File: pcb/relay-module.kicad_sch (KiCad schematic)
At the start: 43 parts, among them J1 AVR-UPDI-6, J2 QWICC, J3 Power In, J4 Power Out, K1 PR24-5V-900-1A, P1 MountingHole_Pad, P2 MountingHole_Pad, P3 MountingHole_Pad, P4 MountingHole_Pad, Q1 MMBT3904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

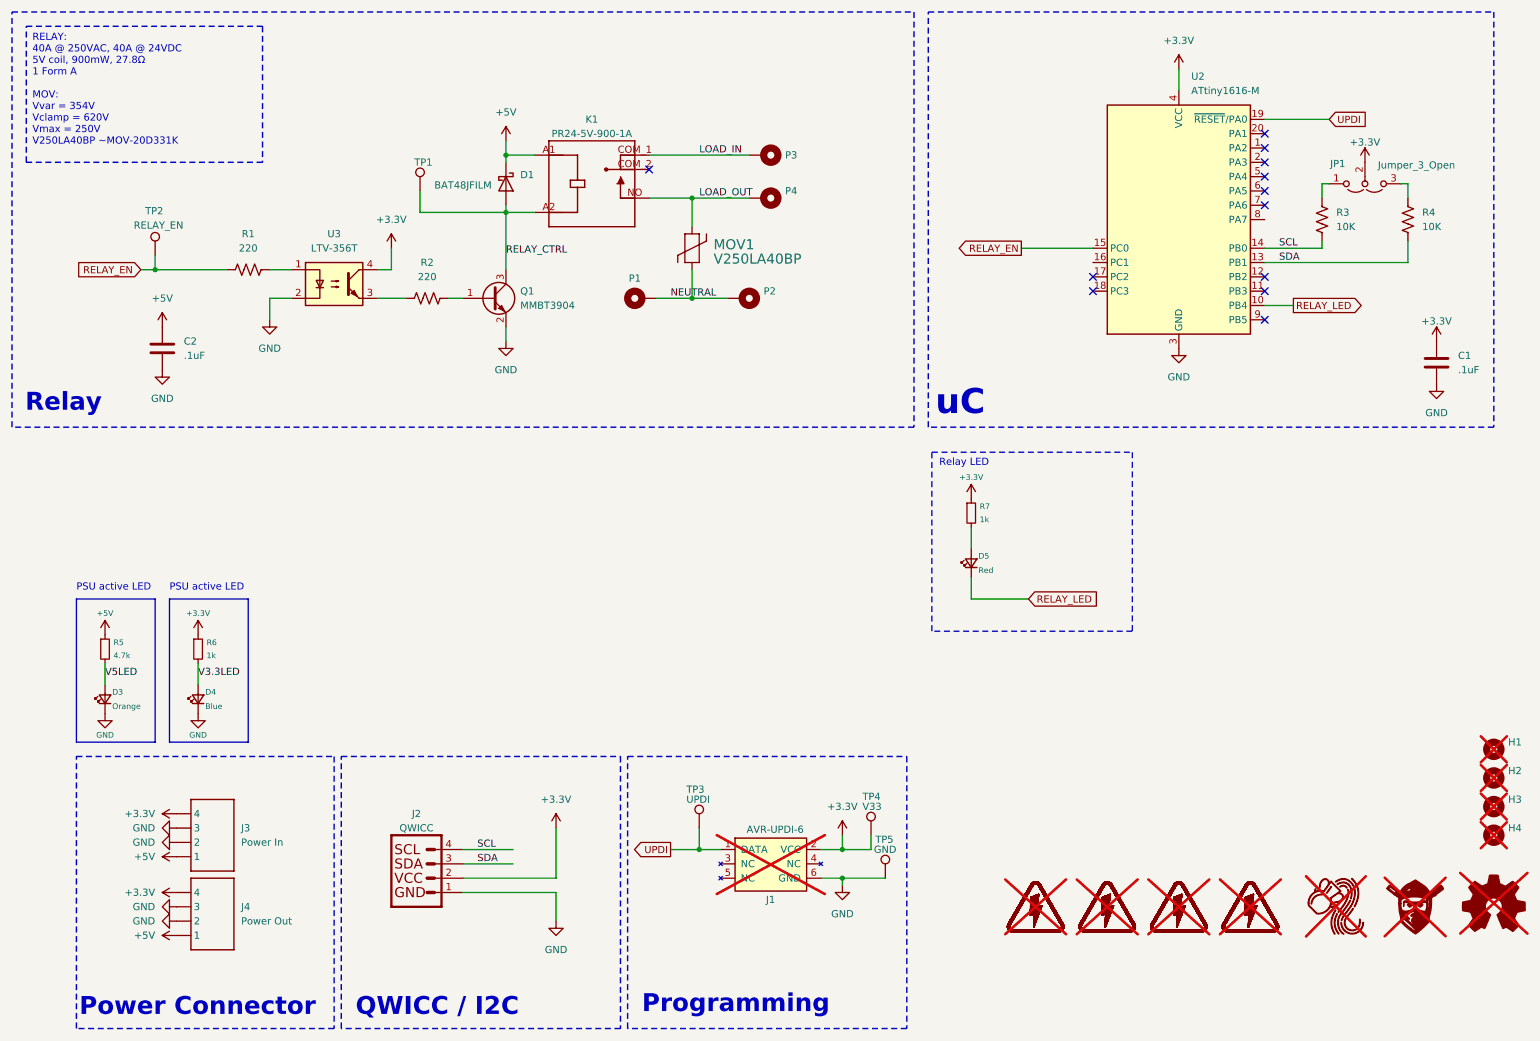
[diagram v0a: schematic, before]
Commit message: Rerouted after adding test points
Added test points to all pins
Added serial connector
Added relay LED
Changed symbols and footprints to CRGM
Moved pins around to optimize routing
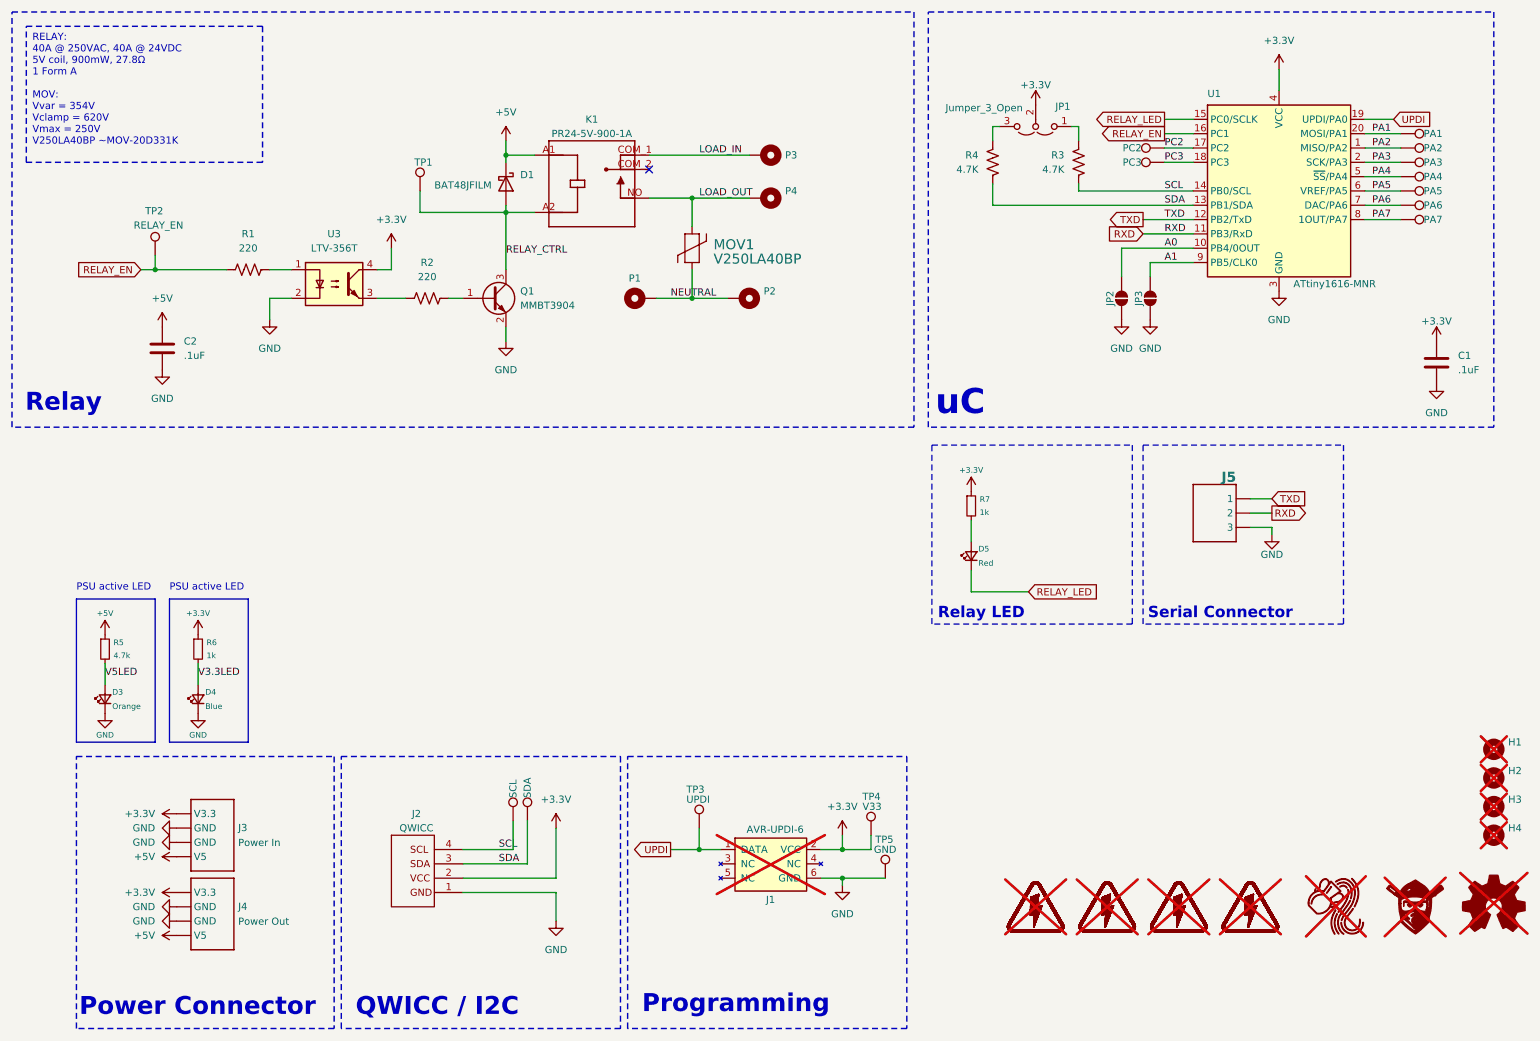
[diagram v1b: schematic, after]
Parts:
- removed U2: ATtiny1616-M, CRG Makes:VQFN-20-1EP_3x3mm_P0.4mm_EP1.7x1.7mm_ThermalVias, symbol MCU_Microchip_ATtiny:ATtiny1616-M
- added J5: ~, Connector_JST:JST_SH_BM03B-SRSS-TB_1x03-1MP_P1.00mm_Vertical, symbol CRGM Connector:JST-SH-3
- added JP2: A0, CRGM Connector:SolderJumper-2_P1.3mm_Open_RoundedPad1.0x1.5mm, symbol Jumper:SolderJumper_2_Open
- added JP3: A1, CRGM Connector:SolderJumper-2_P1.3mm_Open_RoundedPad1.0x1.5mm, symbol Jumper:SolderJumper_2_Open
- added TP10: PA3, CRGM Mechanical:TestPoint_Pad_D1.0mm, symbol Connector:TestPoint
- added TP11: PA4, CRGM Mechanical:TestPoint_Pad_D1.0mm, symbol Connector:TestPoint
- added TP12: PA5, CRGM Mechanical:TestPoint_Pad_D1.0mm, symbol Connector:TestPoint
- added TP13: PA6, CRGM Mechanical:TestPoint_Pad_D1.0mm, symbol Connector:TestPoint
- added TP14: PA7, CRGM Mechanical:TestPoint_Pad_D1.0mm, symbol Connector:TestPoint
- added TP15: SCL, CRGM Mechanical:TestPoint_Pad_D1.0mm, symbol Connector:TestPoint
- added TP16: SDA, CRGM Mechanical:TestPoint_Pad_D1.0mm, symbol Connector:TestPoint
- added TP6: PC2, CRGM Mechanical:TestPoint_Pad_D1.0mm, symbol Connector:TestPoint
- added TP7: PC3, CRGM Mechanical:TestPoint_Pad_D1.0mm, symbol Connector:TestPoint
- added TP8: PA1, CRGM Mechanical:TestPoint_Pad_D1.0mm, symbol Connector:TestPoint
- added TP9: PA2, CRGM Mechanical:TestPoint_Pad_D1.0mm, symbol Connector:TestPoint
- added U1: ATtiny1616-MNR, CRG Makes:VQFN-20-1EP_3x3mm_P0.4mm_EP1.7x1.7mm_ThermalVias, symbol CRG Makes:ATtiny1616-MNR
- J2: MPN SM04B-SRSS-TB -> SM04B-SRSS-TBT(LF)(SN)
- J3, J4: symbol CRGM Connector:JST-SH-4 -> CRGM Connector:AQ_POWER; MPN SM04B-SRSS-TB -> SM04B-SRSS-TBT(LF)(SN)
- JP1: footprint Jumper:SolderJumper-3_P1.3mm_Open_RoundedPad1.0x1.5mm_NumberLabels -> CRGM Connector:SolderJumper-3_P1.3mm_Open_RoundedPad1.0x1.5mm
- R3, R4: value 10K -> 4.7K; Digikey (none) -> 541-3993-2-ND; LCSC C25804 -> C2907166; MN Uni-Royal -> FOJAN; MPN 0603WAF1002T5E -> FRC0603J472 TS; Mouser (none) -> 71-CRCW06034K70JNEAC
- TP1, TP2, TP3, TP4, TP5: footprint TestPoint:TestPoint_Pad_D1.0mm -> CRGM Mechanical:TestPoint_Pad_D1.0mm
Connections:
- net +3.3V: now also U1.4 (VCC)
- net GND: now also J5.3, JP2.1 (A), JP3.1 (A), U1.21 (GND), U1.3 (GND)
- net RELAY_EN: now also U1.16 (PC1)
- net RELAY_LED: now also U1.15 (PC0/SCLK)
- net SCL: now also TP15.1, U1.14 (PB0/SCL)
- net SDA: now also TP16.1, U1.13 (PB1/SDA)
- net UPDI: now also U1.19 (UPDI/PA0)
- new net A0: JP2.2 (B), U1.10 (PB4/0OUT)
- new net A1: JP3.2 (B), U1.9 (PB5/CLK0)
- new net PA1: TP8.1, U1.20 (MOSI/PA1)
- new net PA2: TP9.1, U1.1 (MISO/PA2)
- new net PA3: TP10.1, U1.2 (SCK/PA3)
- new net PA4: TP11.1, U1.5 (~{SS}/PA4)
- new net PA5: TP12.1, U1.6 (VREF/PA5)
- new net PA6: TP13.1, U1.7 (DAC/PA6)
- new net PA7: TP14.1, U1.8 (1OUT/PA7)
- new net PC2: TP6.1, U1.17 (PC2)
- new net PC3: TP7.1, U1.18 (PC3)
- new net RXD: J5.2, U1.11 (PB3/RxD)
- new net TXD: J5.1, U1.12 (PB2/TxD)
- no-connect marks 12 -> 1
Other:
- note added: "Serial Connector"
- moved on the sheet: D5, JP1, R3, R4, R7

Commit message: schematic and PCB clean up
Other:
- note added: "Power LEDs"
- note removed: "PSU active LED"
- moved on the sheet: D3, D4, D5, J1, J2, J3, J4, J5, R5, R6, R7, TP3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

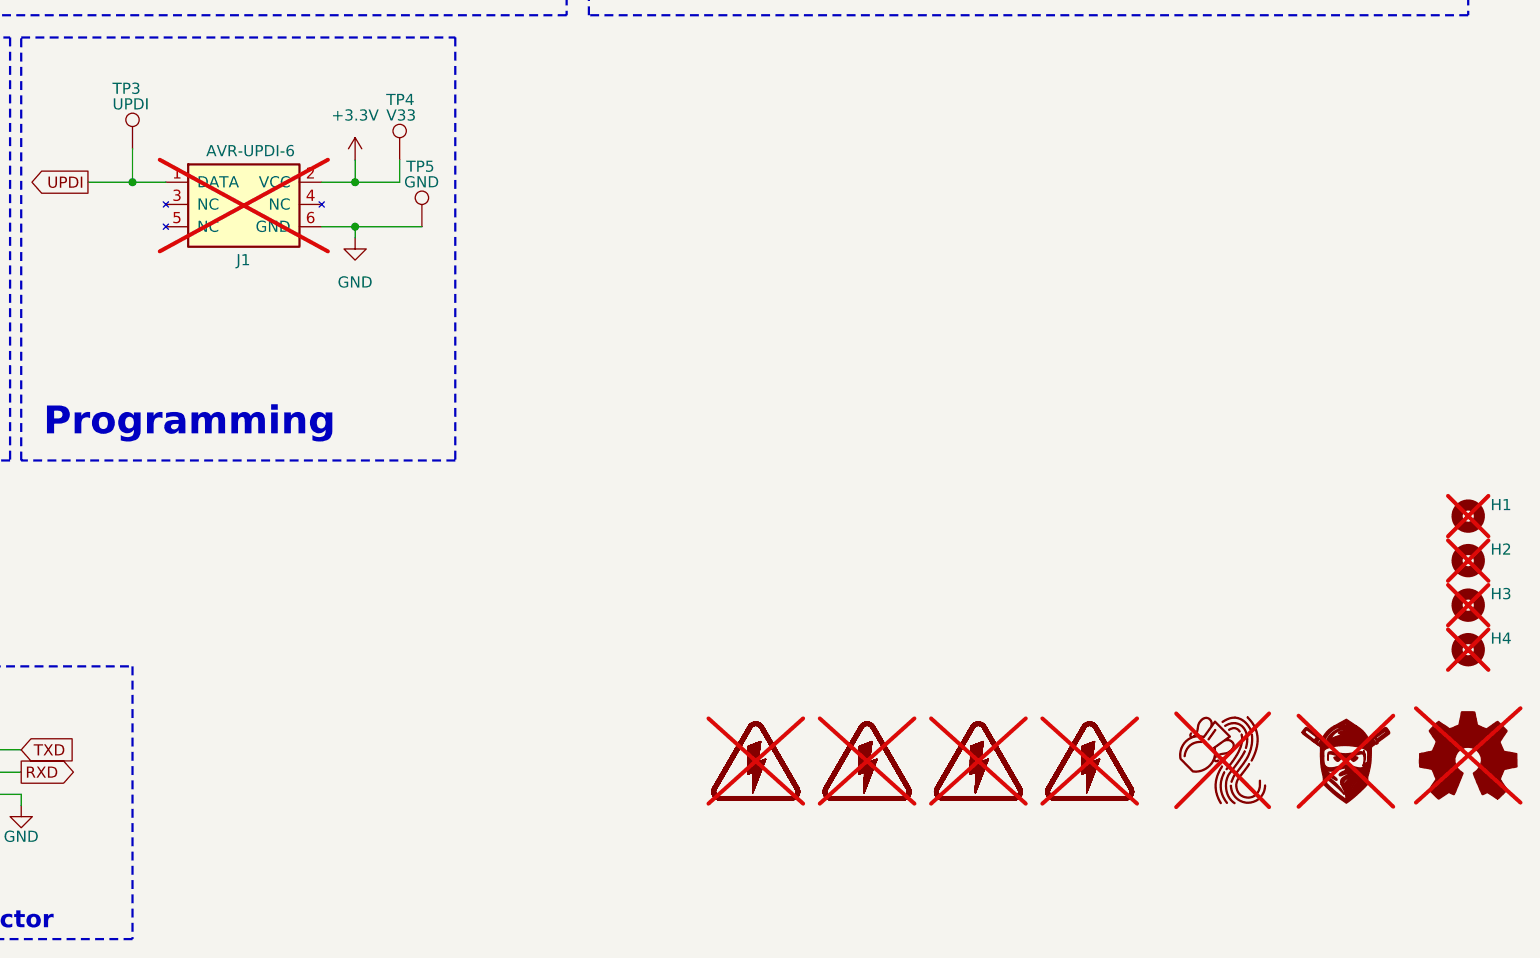
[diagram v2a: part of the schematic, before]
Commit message: Updated mounting holes; rounded corners
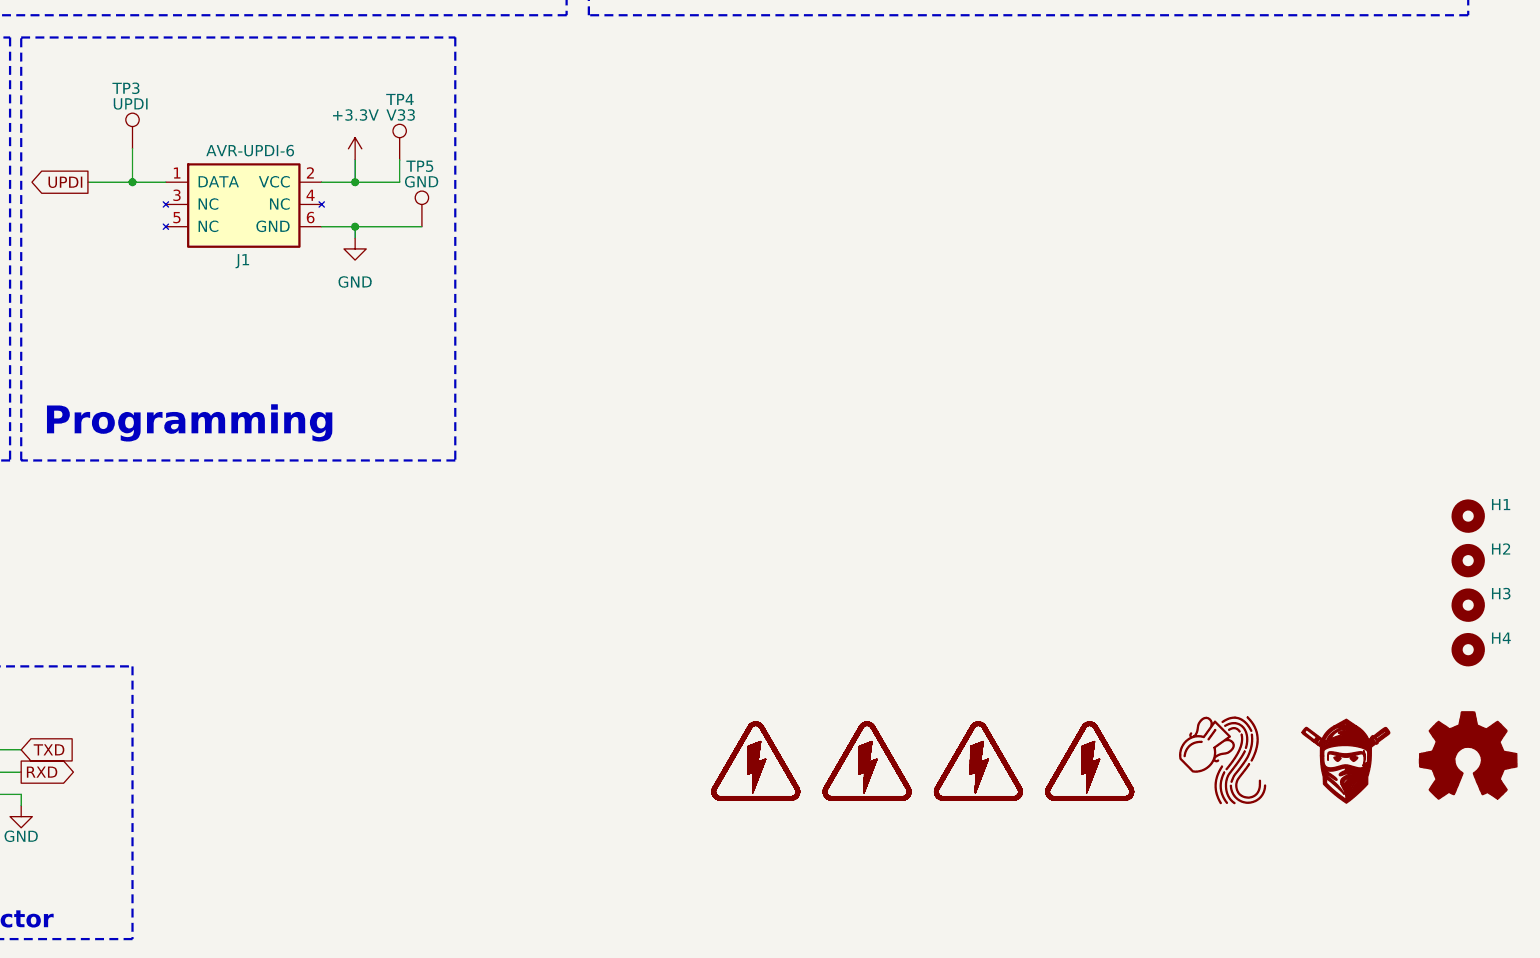
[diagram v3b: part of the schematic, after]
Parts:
- H1, H2, H3, H4, J1, LOGO1, LOGO3, LOGO5, S1, S2, S3, S4: now fitted
- P1, P2, P3, P4: footprint MountingHole:MountingHole_3.2mm_M3_ISO14580_Pad -> CRGM Mechanical:MountingHole_3.2mm_M3_ISO14580_Pad
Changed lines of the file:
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@@
 		(in_bom no)
 		(on_board yes)
-		(dnp yes)
+		(dnp no)
 		(fields_autoplaced yes)
 		(property "Reference" "H1"
@@
 		(in_bom no)
 		(on_board yes)
-		(dnp yes)
+		(dnp no)
 		(fields_autoplaced yes)
 		(property "Reference" "S3"
@@
 		(in_bom no)
 		(on_board yes)
-		(dnp yes)
+		(dnp no)
 		(fields_autoplaced yes)
 		(property "Reference" "LOGO1"
@@
 			)
 		)
-		(property "Footprint" "MountingHole:MountingHole_3.2mm_M3_ISO14580_Pad"
+		(property "Footprint" "CRGM Mechanical:MountingHole_3.2mm_M3_ISO14580_Pad"
 			(at 148.59 40.64 0)
 			(effects
@@
 		(in_bom no)
 		(on_board yes)
-		(dnp yes)
+		(dnp no)
 		(fields_autoplaced yes)
 		(property "Reference" "S2"
@@
 		(in_bom no)
 		(on_board yes)
-		(dnp yes)
+		(dnp no)
 		(property "Reference" "J1"
 			(at 139.192 116.84 0)
@@
 		(in_bom no)
 		(on_board yes)
-		(dnp yes)
+		(dnp no)
 		(fields_autoplaced yes)
 		(property "Reference" "H3"
@@
 		(in_bom no)
 		(on_board yes)
-		(dnp yes)
+		(dnp no)
 		(fields_autoplaced yes)
 		(property "Reference" "LOGO5"
@@
 		(in_bom no)
 		(on_board yes)
-		(dnp yes)
+		(dnp no)
 		(fields_autoplaced yes)
 		(property "Reference" "LOGO3"
@@
 		(in_bom no)
 		(on_board yes)
-		(dnp yes)
+		(dnp no)
 		(fields_autoplaced yes)
 		(property "Reference" "S4"
@@
 		(in_bom no)
 		(on_board yes)
-		(dnp yes)
+		(dnp no)
 		(fields_autoplaced yes)
 		(property "Reference" "H2"
@@
 			)
 		)
-		(property "Footprint" "MountingHole:MountingHole_3.2mm_M3_ISO14580_Pad"
+		(property "Footprint" "CRGM Mechanical:MountingHole_3.2mm_M3_ISO14580_Pad"
 			(at 148.59 48.26 0)
 			(effects
@@
 		(in_bom no)
 		(on_board yes)
-		(dnp yes)
+		(dnp no)
 		(fields_autoplaced yes)
 		(property "Reference" "S1"
@@
 		(in_bom no)
 		(on_board yes)
-		(dnp yes)
+		(dnp no)
 		(fields_autoplaced yes)
 		(property "Reference" "H4"
@@
 			)
 		)
-		(property "Footprint" "MountingHole:MountingHole_3.2mm_M3_ISO14580_Pad"
+		(property "Footprint" "CRGM Mechanical:MountingHole_3.2mm_M3_ISO14580_Pad"
 			(at 127 66.04 0)
 			(effects
@@
 			)
 		)
-		(property "Footprint" "MountingHole:MountingHole_3.2mm_M3_ISO14580_Pad"
+		(property "Footprint" "CRGM Mechanical:MountingHole_3.2mm_M3_ISO14580_Pad"
 			(at 144.78 66.04 0)
 			(effects
